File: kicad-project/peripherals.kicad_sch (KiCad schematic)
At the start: 10 parts

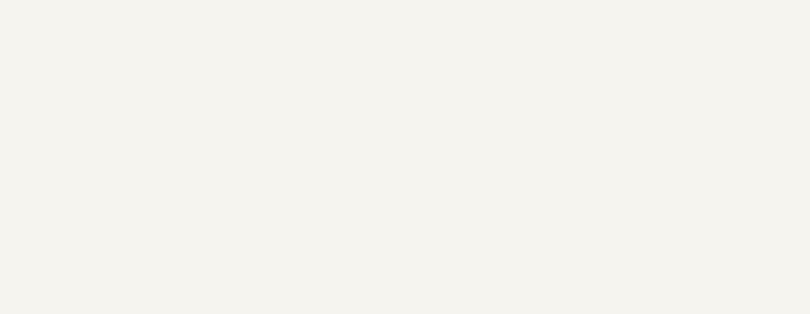
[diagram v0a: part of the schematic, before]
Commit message: hw: add power managment
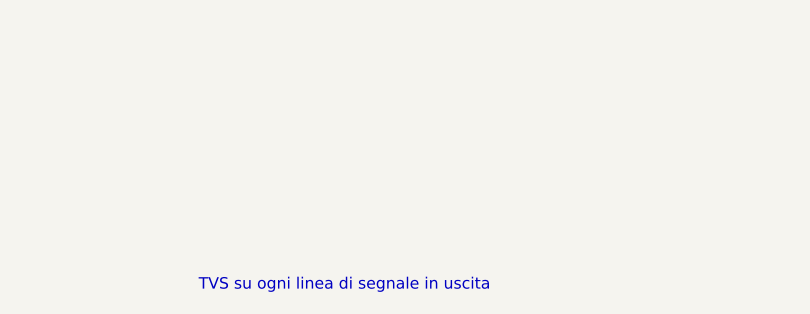
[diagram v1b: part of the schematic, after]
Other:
- note added: "TVS su ogni linea di segnale in uscita"
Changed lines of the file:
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@@
     (effects (font (size 3 3) (thickness 0.6) bold) (justify right bottom))
+  )
+  (text "TVS su ogni linea di segnale in uscita\n" (at 93.98 187.96 0)
+    (effects (font (size 1.27 1.27)) (justify left bottom))
   )
   (text "LED Alive\n" (at 168.91 31.75 0)

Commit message: hw: update
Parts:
- removed R? (x2): R, Resistor_SMD:R_0603_1608Metric, symbol Device:R
- added Q? (x3): BC846A, Package_TO_SOT_SMD:SOT-23, symbol Device:Q_NPN_BCE
- added R? (x2): 470, Resistor_SMD:R_0603_1608Metric, symbol Device:R
- added R? (x3): 33k, Resistor_SMD:R_0603_1608Metric, symbol Device:R
- R?: value R -> 470
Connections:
- net ~{iLED_B}: now also R?.1
- net ~{iLED_R}: now also R?.1
- net ~{LED_G}: no longer names the net of R?.2
- net ~{LED_G}: now also Q?.3 (E)
- new net: Q?.1 (B), R?.2 (x3)
- new net: Q?.3 (E), R?.2 (x2)
- new net +5V: Q?.2 (C), Q?.2 (C), Q?.2 (C)
- new net LED_B: R?.1
- new net LED_G: R?.1
- new net LED_R: R?.1
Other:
- note added: "c'è led blu, quindi 3v3 non basta"
- note removed: "Alimentazione da definire, c'è led blu, quindi 3v3 non basta"
- moved on the sheet: D?, J?, R?

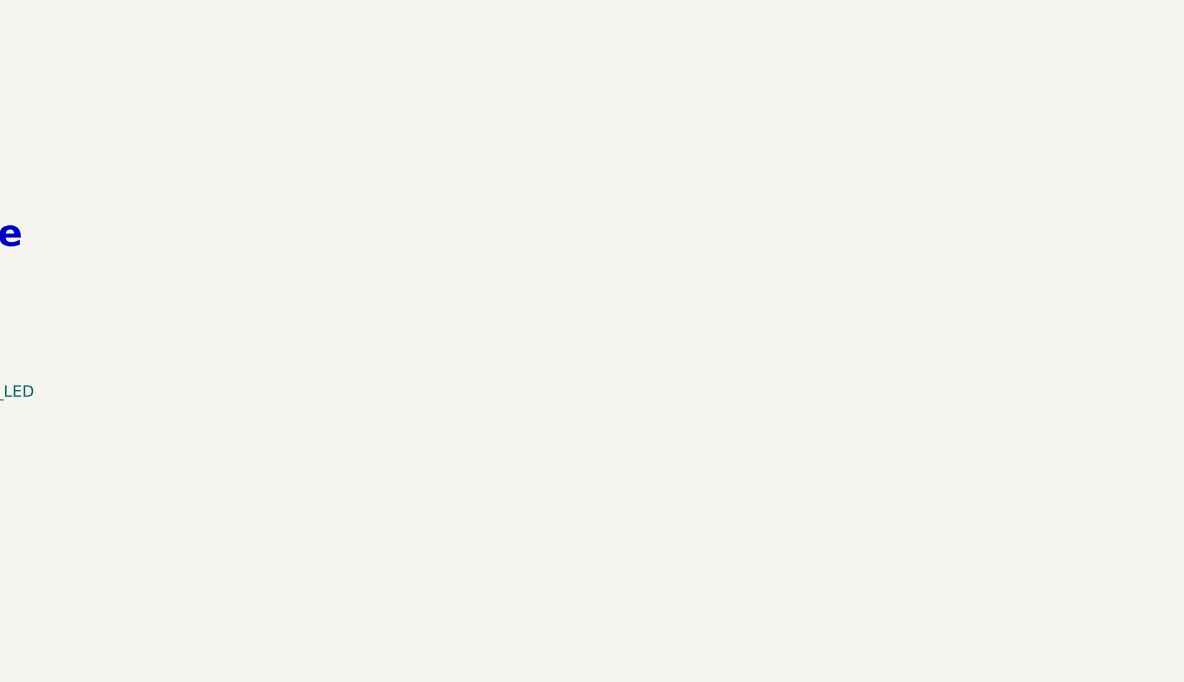
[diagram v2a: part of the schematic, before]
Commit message: hw: add esp8266
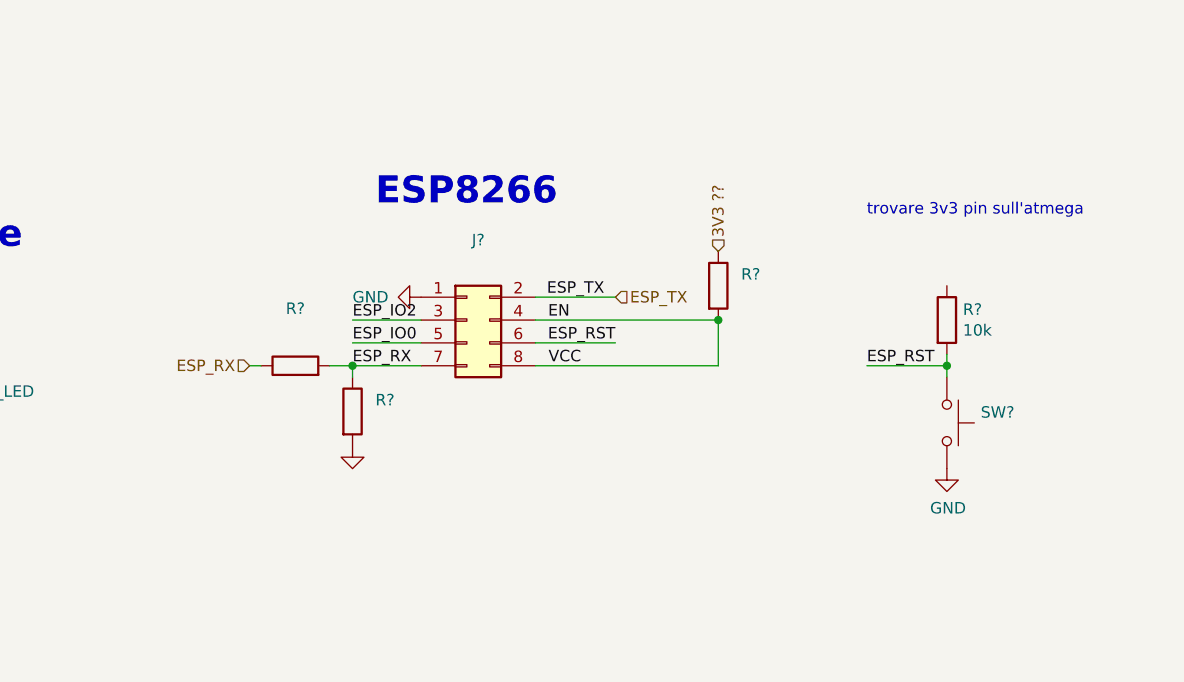
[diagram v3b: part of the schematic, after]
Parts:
- added J?: (no value), symbol Connector_Generic:Conn_02x04_Odd_Even
- added R?: 10k, Resistor_SMD:R_0603_1608Metric, symbol Device:R
- added R? (x3): (no value), symbol Device:R
- added SW?: (no value), Button_Switch_THT:SW_PUSH_6mm, symbol Switch:SW_Push
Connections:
- net GND: now also J?.1 (Pin_1), R?.2, SW?.2
- new net 3V3 ??: R?.1
- new net EN: J?.4 (Pin_4), J?.8 (Pin_8), R?.2
- new net ESP_IO0: J?.5 (Pin_5)
- new net ESP_IO2: J?.3 (Pin_3)
- new net ESP_RST: J?.6 (Pin_6), R?.2, SW?.1
- new net ESP_RX: J?.7 (Pin_7), R?.1, R?.1, R?.2
- new net ESP_TX: J?.2 (Pin_2)
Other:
- note added: "ESP8266"
- note added: "trovare 3v3 pin sull'atmega"

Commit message: hw: change to rp2040
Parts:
- removed Q? (x3): BC846A, Package_TO_SOT_SMD:SOT-23, symbol Device:Q_NPN_BCE
- removed Q?: PDTC114Y, symbol Transistor_BJT:DTC114Y
- added Q? (x4): S8050, Package_TO_SOT_SMD:SOT-23, symbol Device:Q_NPN_BEC
- added R?: 10k, symbol Device:R
- added R?: 47k, symbol Device:R
- J?: value (none) -> Conn_02x04_Odd_Even
- R?: value 330 -> 470
- R? (x2): value (none) -> 1K
- R?: value (none) -> 10k
- SW?: value (none) -> ESP_RST_SW; footprint Button_Switch_THT:SW_PUSH_6mm -> Button_Switch_THT:SW_PUSH_6mm_H4.3mm
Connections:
- net +3V3 is gone; now on net +5V: BZ?.1 (-), D?.2 (A), J?.2 (Pin_2), R?.1
- net +5V: now also Q?.3 (C), Q?.3 (C), Q?.3 (C)
- net Buzzer: now also R?.1
- net GND: now also Q?.2 (E), R?.2
- net iBuzzer: now also Q?.3 (C)
- net at R?.2: now also Q?.1 (B) (x3)
- net at R?.2: now also Q?.2 (E) (x3)
- new net: Q?.1 (B), R?.1, R?.2

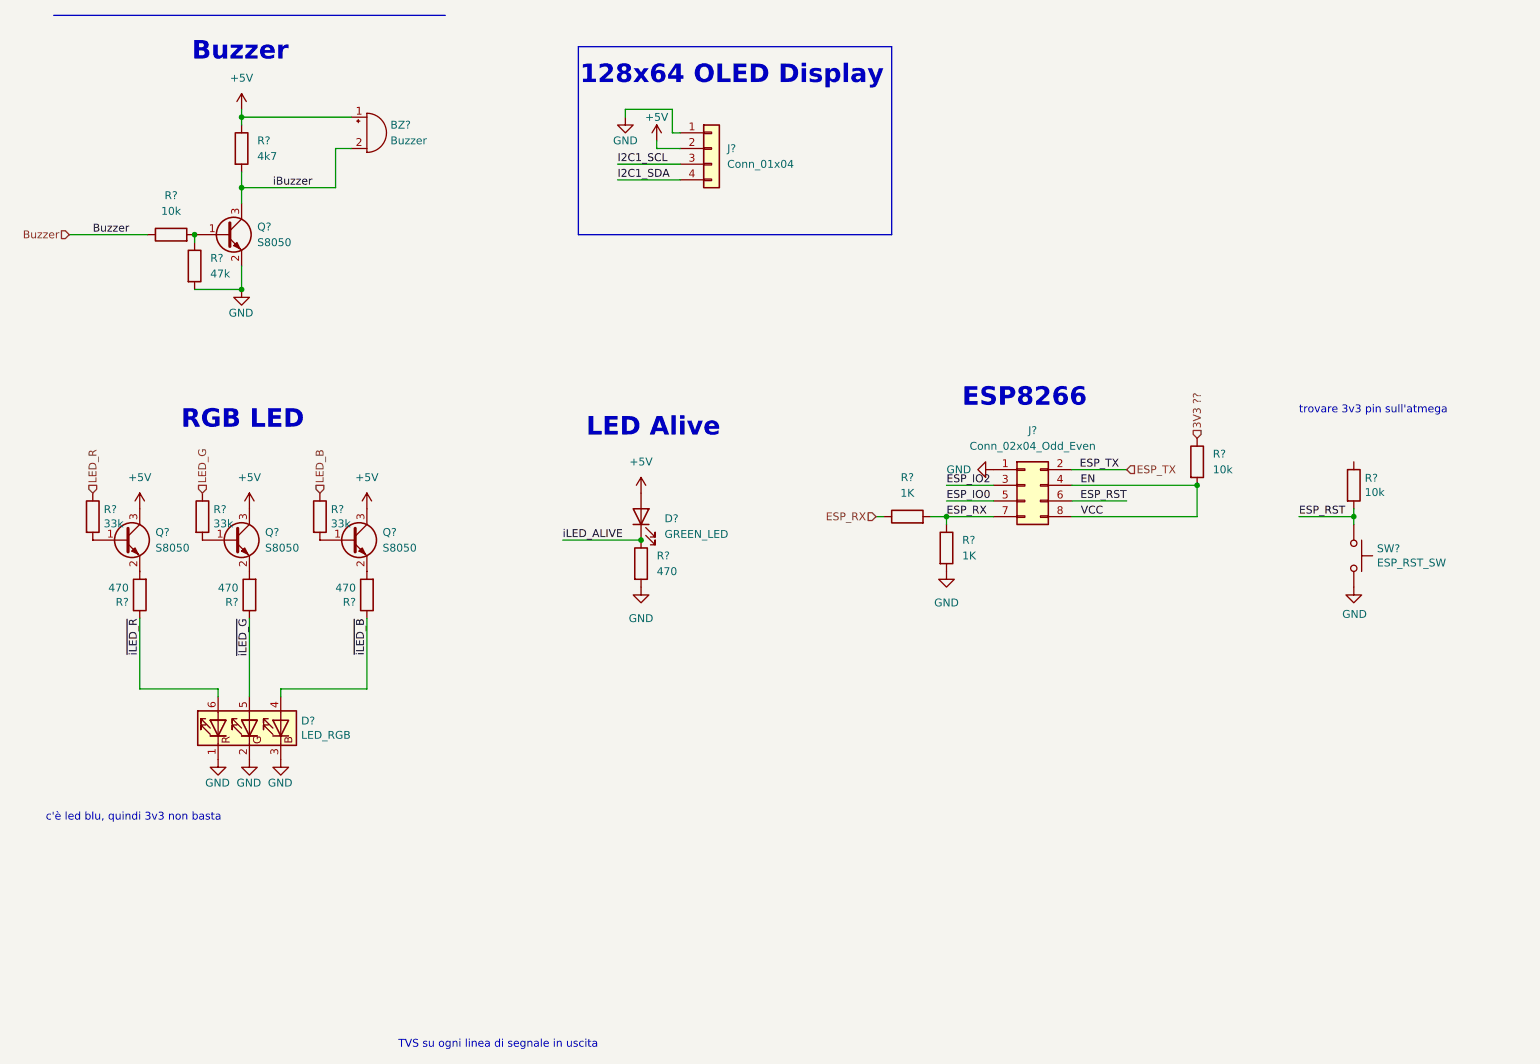
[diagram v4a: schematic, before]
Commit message: hw: change power management and drivers
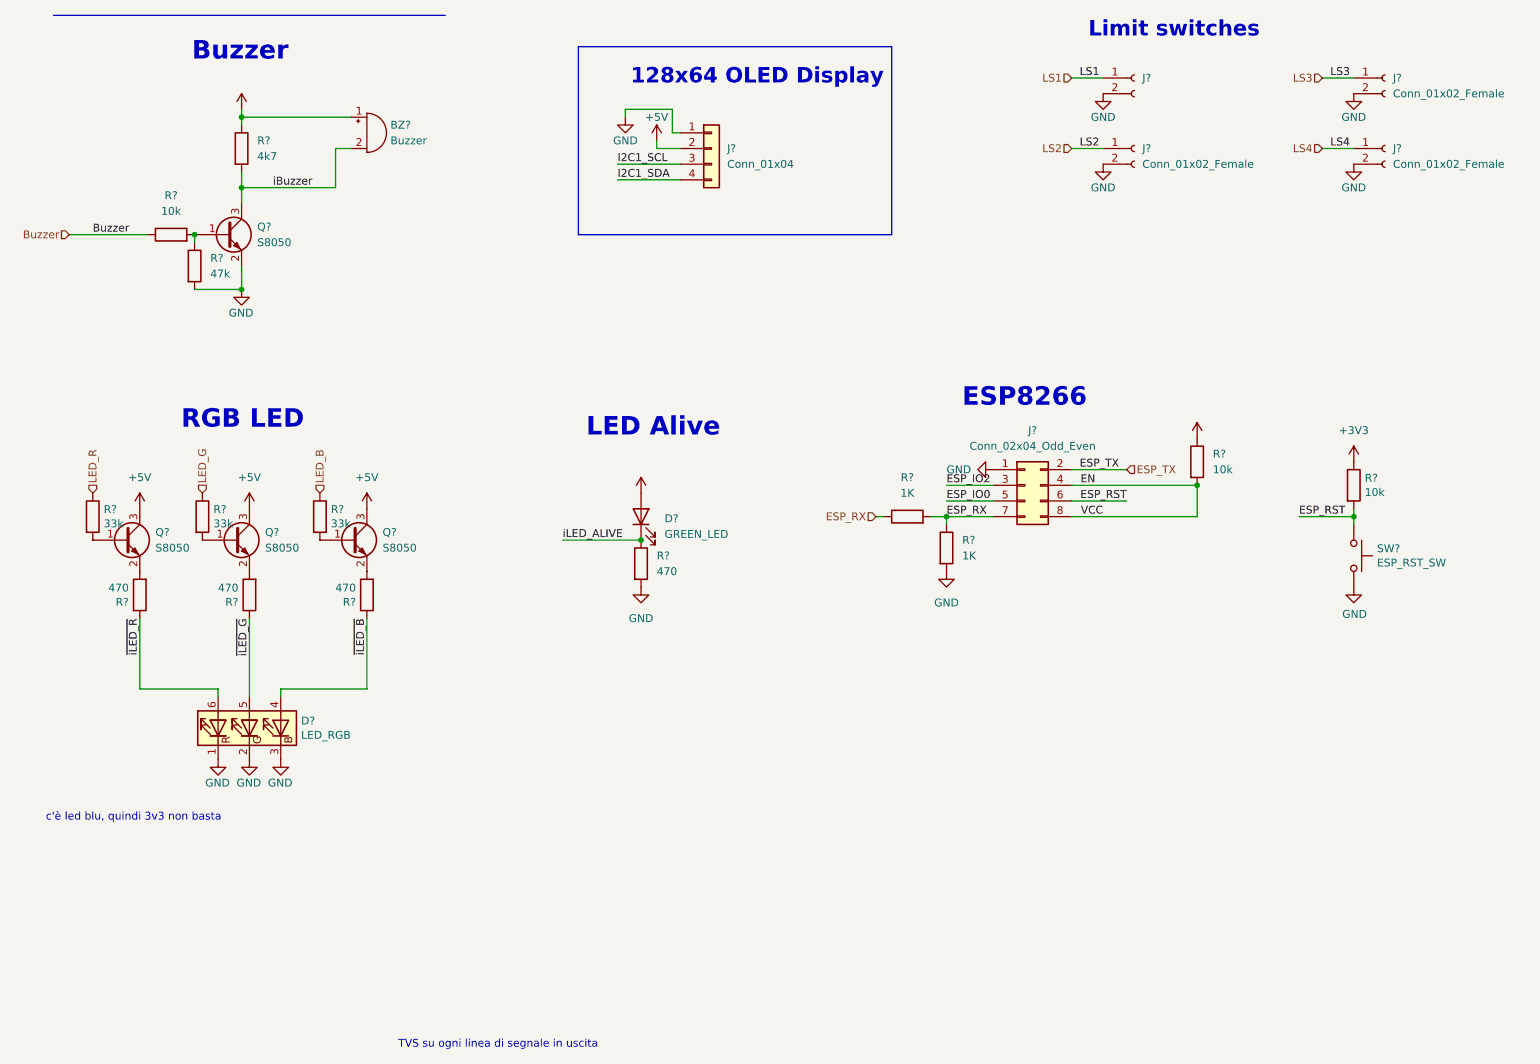
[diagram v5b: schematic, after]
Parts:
- added J? (x3): Conn_01x02_Female, symbol Connector:Conn_01x02_Female
- added J?: (no value), symbol Connector:Conn_01x02_Female
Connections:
- net 3V3 ?? is gone; now on net +3V3: R?.1
- net +5V: no longer BZ?.1 (-), D?.2 (A), R?.1
- net GND: now also J?.2 (Pin_2), J?.2 (Pin_2), J?.2 (Pin_2), J?.2 (Pin_2)
- net +3V3: now reaches R?.1
- net +3V3: now also BZ?.1 (-), D?.2 (A), R?.1
- new net LS1: J?.1 (Pin_1)
- new net LS2: J?.1 (Pin_1)
- new net LS3: J?.1 (Pin_1)
- new net LS4: J?.1 (Pin_1)
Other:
- note added: "Limit switches"
- note removed: "trovare 3v3 pin sull'atmega"

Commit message: Bipolar pins
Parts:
- J?: value (none) -> Conn_01x02_Female
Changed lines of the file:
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@@
       (effects (font (size 1.27 1.27)) hide)
     )
-    (property "Value" "" (id 1) (at 68.58 30.48 0))
+    (property "Value" "+3V3" (id 1) (at 68.58 30.48 0))
     (property "Footprint" "" (id 2) (at 68.58 35.56 0)
       (effects (font (size 1.27 1.27)) hide)
@@
       (effects (font (size 1.27 1.27)) hide)
     )
-    (property "Value" "" (id 1) (at 223.52 83.82 0))
+    (property "Value" "+3V3" (id 1) (at 223.52 83.82 0))
     (property "Footprint" "" (id 2) (at 223.52 88.9 0)
       (effects (font (size 1.27 1.27)) hide)
@@
       (effects (font (size 1.27 1.27)) hide)
     )
-    (property "Value" "" (id 1) (at 133.35 92.71 0))
+    (property "Value" "+3V3" (id 1) (at 133.35 92.71 0))
     (property "Footprint" "" (id 2) (at 133.35 97.79 0)
       (effects (font (size 1.27 1.27)) hide)
@@
       (effects (font (size 1.27 1.27)) (justify left))
     )
-    (property "Value" "" (id 1) (at 214.63 33.0199 0)
-      (effects (font (size 1.27 1.27)) (justify left))
-    )
+    (property "Value" "Conn_01x02_Female" (id 1) (at 214.63 33.0199 0)
+      (effects (font (size 1.27 1.27)) (justify left))
+    )
